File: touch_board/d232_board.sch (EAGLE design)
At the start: 42 parts, among them IC1 uln2803, IC2 uln2803, IC3_5V 7805TV, IC4_10V 7805TV, IC5_12V 7805TV, X1 057-050-1

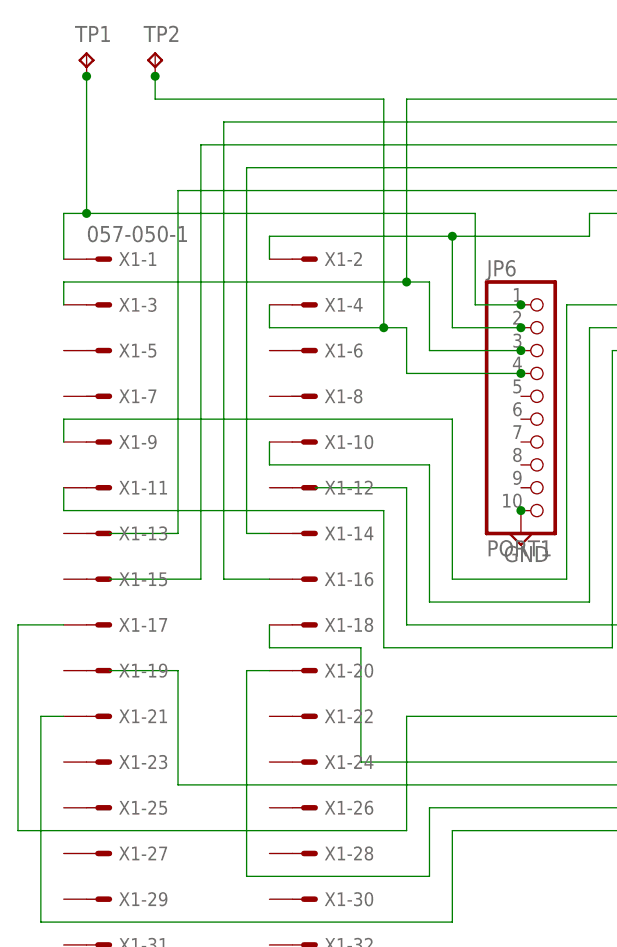
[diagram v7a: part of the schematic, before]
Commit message: fix missing traces to conector
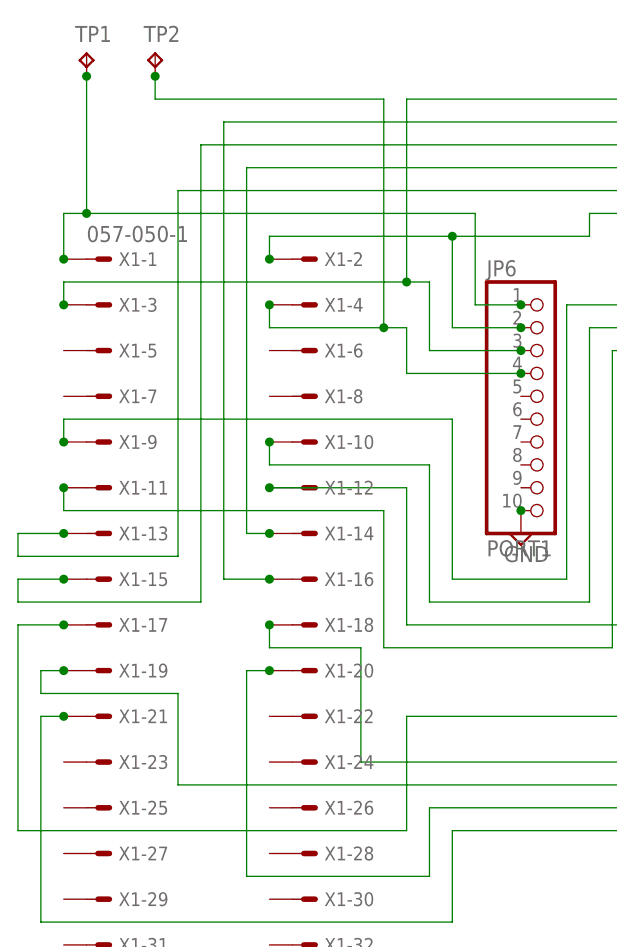
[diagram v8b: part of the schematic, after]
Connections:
- net N$12: now also X1-12.S
- net N$13: now also X1-13.S
- net N$15: now also X1-15.S
- net N$19: now also X1-19.S
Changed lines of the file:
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@@
 <wire x1="-10.16" y1="81.28" x2="10.16" y2="81.28" width="0.1524" layer="91"/>
 <junction x="10.16" y="81.28"/>
+<junction x="-66.04" y="66.04"/>
 </segment>
 </net>
@@
 <wire x1="-7.62" y1="78.74" x2="10.16" y2="78.74" width="0.1524" layer="91"/>
 <junction x="10.16" y="78.74"/>
+<junction x="-43.18" y="66.04"/>
 </segment>
 </net>
@@
 <wire x1="-5.08" y1="76.2" x2="10.16" y2="76.2" width="0.1524" layer="91"/>
 <junction x="10.16" y="76.2"/>
+<junction x="-66.04" y="60.96"/>
 </segment>
 </net>
@@
 <wire x1="10.16" y1="73.66" x2="27.94" y2="73.66" width="0.1524" layer="91"/>
 <junction x="27.94" y="73.66"/>
-<wire x1="-38.1" y1="60.96" x2="-27.94" y2="60.96" width="0.1524" layer="91"/>
 <wire x1="-27.94" y1="60.96" x2="-27.94" y2="45.72" width="0.1524" layer="91"/>
 <wire x1="-27.94" y1="45.72" x2="-2.54" y2="45.72" width="0.1524" layer="91"/>
@@
 <wire x1="-2.54" y1="73.66" x2="10.16" y2="73.66" width="0.1524" layer="91"/>
 <junction x="10.16" y="73.66"/>
+<pinref part="X1" gate="-12" pin="S"/>
+<wire x1="-27.94" y1="60.96" x2="-43.18" y2="60.96" width="0.1524" layer="91"/>
+<junction x="-43.18" y="60.96"/>
 </segment>
 </net>
@@
 <wire x1="10.16" y1="71.12" x2="27.94" y2="71.12" width="0.1524" layer="91"/>
 <junction x="27.94" y="71.12"/>
-<wire x1="-60.96" y1="55.88" x2="-53.34" y2="55.88" width="0.1524" layer="91"/>
-<wire x1="-53.34" y1="55.88" x2="-53.34" y2="93.98" width="0.1524" layer="91"/>
+<wire x1="-53.34" y1="53.34" x2="-53.34" y2="93.98" width="0.1524" layer="91"/>
 <wire x1="-53.34" y1="93.98" x2="-2.54" y2="93.98" width="0.1524" layer="91"/>
 <wire x1="-2.54" y1="93.98" x2="-2.54" y2="88.9" width="0.1524" layer="91"/>
@@
 <wire x1="0" y1="71.12" x2="10.16" y2="71.12" width="0.1524" layer="91"/>
 <junction x="10.16" y="71.12"/>
+<pinref part="X1" gate="-13" pin="S"/>
+<wire x1="-66.04" y1="55.88" x2="-71.12" y2="55.88" width="0.1524" layer="91"/>
+<wire x1="-71.12" y1="55.88" x2="-71.12" y2="53.34" width="0.1524" layer="91"/>
+<wire x1="-71.12" y1="53.34" x2="-53.34" y2="53.34" width="0.1524" layer="91"/>
+<junction x="-66.04" y="55.88"/>
 </segment>
 </net>
@@
 <wire x1="2.54" y1="68.58" x2="10.16" y2="68.58" width="0.1524" layer="91"/>
 <junction x="10.16" y="68.58"/>
+<junction x="-43.18" y="55.88"/>
 </segment>
 </net>
@@
 <wire x1="27.94" y1="66.04" x2="30.48" y2="66.04" width="0.1524" layer="91"/>
 <junction x="27.94" y="66.04"/>
-<wire x1="-60.96" y1="50.8" x2="-50.8" y2="50.8" width="0.1524" layer="91"/>
-<wire x1="-50.8" y1="50.8" x2="-50.8" y2="99.06" width="0.1524" layer="91"/>
+<wire x1="-50.8" y1="48.26" x2="-50.8" y2="99.06" width="0.1524" layer="91"/>
 <wire x1="-50.8" y1="99.06" x2="17.78" y2="99.06" width="0.1524" layer="91"/>
 <wire x1="17.78" y1="99.06" x2="17.78" y2="66.04" width="0.1524" layer="91"/>
 <junction x="17.78" y="66.04"/>
 <junction x="10.16" y="66.04"/>
+<pinref part="X1" gate="-15" pin="S"/>
+<wire x1="-66.04" y1="50.8" x2="-71.12" y2="50.8" width="0.1524" layer="91"/>
+<wire x1="-71.12" y1="50.8" x2="-71.12" y2="48.26" width="0.1524" layer="91"/>
+<wire x1="-71.12" y1="48.26" x2="-50.8" y2="48.26" width="0.1524" layer="91"/>
+<junction x="-66.04" y="50.8"/>
 </segment>
 </net>
@@
 <junction x="20.32" y="63.5"/>
 <junction x="10.16" y="63.5"/>
+<junction x="-43.18" y="50.8"/>
 </segment>
 </net>
@@
 <wire x1="5.08" y1="33.02" x2="10.16" y2="33.02" width="0.1524" layer="91"/>
 <junction x="10.16" y="33.02"/>
+<junction x="-66.04" y="45.72"/>
 </segment>
 </net>
@@
 <wire x1="-33.02" y1="30.48" x2="10.16" y2="30.48" width="0.1524" layer="91"/>
 <junction x="10.16" y="30.48"/>
+<junction x="-43.18" y="45.72"/>
 </segment>
 </net>
@@
 <junction x="27.94" y="27.94"/>
 <wire x1="27.94" y1="27.94" x2="30.48" y2="27.94" width="0.1524" layer="91"/>
-<wire x1="-60.96" y1="40.64" x2="-53.34" y2="40.64" width="0.1524" layer="91"/>
-<wire x1="-53.34" y1="40.64" x2="-53.34" y2="27.94" width="0.1524" layer="91"/>
+<wire x1="-53.34" y1="38.1" x2="-53.34" y2="27.94" width="0.1524" layer="91"/>
 <wire x1="-53.34" y1="27.94" x2="10.16" y2="27.94" width="0.1524" layer="91"/>
 <junction x="10.16" y="27.94"/>
+<pinref part="X1" gate="-19" pin="S"/>
+<wire x1="-66.04" y1="40.64" x2="-68.58" y2="40.64" width="0.1524" layer="91"/>
+<wire x1="-68.58" y1="40.64" x2="-68.58" y2="38.1" width="0.1524" layer="91"/>
+<wire x1="-68.58" y1="38.1" x2="-53.34" y2="38.1" width="0.1524" layer="91"/>
+<junction x="-66.04" y="40.64"/>
 </segment>
 </net>
@@
 <wire x1="-25.4" y1="25.4" x2="10.16" y2="25.4" width="0.1524" layer="91"/>
 <junction x="10.16" y="25.4"/>
+<junction x="-43.18" y="40.64"/>
 </segment>
 </net>
@@
 <wire x1="-22.86" y1="22.86" x2="10.16" y2="22.86" width="0.1524" layer="91"/>
 <junction x="10.16" y="22.86"/>
+<junction x="-66.04" y="35.56"/>
 </segment>
 </net>
@@
 <junction x="-63.5" y="91.44"/>
 <junction x="-63.5" y="106.68"/>
+<junction x="-66.04" y="86.36"/>
 </segment>
 </net>
@@
 <wire x1="35.56" y1="91.44" x2="-7.62" y2="91.44" width="0.1524" layer="91"/>
 <junction x="-22.86" y="88.9"/>
+<junction x="-43.18" y="86.36"/>
 </segment>
 </net>
@@
 <pinref part="R10" gate="G$1" pin="1"/>
 <junction x="-27.94" y="83.82"/>
+<junction x="-66.04" y="81.28"/>
 </segment>
 </net>
@@
 <junction x="-30.48" y="78.74"/>
 <junction x="-55.88" y="106.68"/>
-</segment>
-</net>
+<junction x="-43.18" y="81.28"/>
+</segment>
+</net>
